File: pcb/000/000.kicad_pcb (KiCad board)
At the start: 4 copper layers, 80 x 71 mm, 155 parts, among them J1 Screw_Terminal_01x10, J2 Screw_Terminal_01x10, Q1 BC846BLT1G, Q10 BC846BLT1G, Q11 BC846BLT1G, Q12 BC846BLT1G, Q13 BC846BLT1G, Q14 BC846BLT1G, Q15 BC846BLT1G, Q16 BC846BLT1G, Q17 BC846BLT1G, Q18 BC846BLT1G, Q19 BC846BLT1G, Q2 BC846BLT1G, Q20 BC846BLT1G, Q21 BC846BLT1G, Q22 BC846BLT1G, Q23 BC846BLT1G, Q24 BC846BLT1G, Q3 BC846BLT1G, Q4 BC846BLT1G, Q5 BC846BLT1G, Q6 BC846BLT1G, Q7 BC846BLT1G, Q8 BC846BLT1G, Q9 BC846BLT1G, SW1 SW_DIP_x08, U1 LM339, U2 LM339, U3 TLP291-4, U4 TLP291-4, U5 RFM-0505S

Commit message: rev 4 commit, works but uses a lot of power. commiting this change before going over to the new design
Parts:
- added J3: Conn_01x03, Connector_PinHeader_2.54mm:PinHeader_1x03_P2.54mm_Vertical, F.Cu at (162.0, 116.8)
- added R69: 10kOhm, Resistor_SMD:R_0603_1608Metric, F.Cu at (168.2, 109.5)
- added R70: 20kOhm, Resistor_SMD:R_0603_1608Metric, F.Cu at (166.8, 109.5)
- moved C3 0.50 mm to (167.8, 104.5)
- moved C4 0.50 mm to (159.5, 103.8)
- moved C5 0.50 mm to (159.5, 112.8)
- moved L1 0.50 mm to (164.2, 103.5)
- moved U5 0.50 mm to (159.5, 108.2)
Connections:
- R59 pad 1: ISO_VCC -> PULLUP
- R60 pad 1: ISO_VCC -> PULLUP
- R61 pad 1: ISO_VCC -> PULLUP
- R62 pad 1: ISO_VCC -> PULLUP
- R63 pad 1: ISO_VCC -> PULLUP
- R64 pad 1: ISO_VCC -> PULLUP
- R65 pad 1: ISO_VCC -> PULLUP
- R66 pad 1: ISO_VCC -> PULLUP
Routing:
- net PULLUP: track 0.00 -> 38.8 mm, vias 0 -> 8
- net ISO_3.3: track 0.00 -> 16.6 mm
- net ISO_GND: track 43.8 -> 46.2 mm
- net GND: track 50.6 -> 51.5 mm
- net ISO_VCC: track 17.1 -> 16.3 mm, vias 9 -> 3

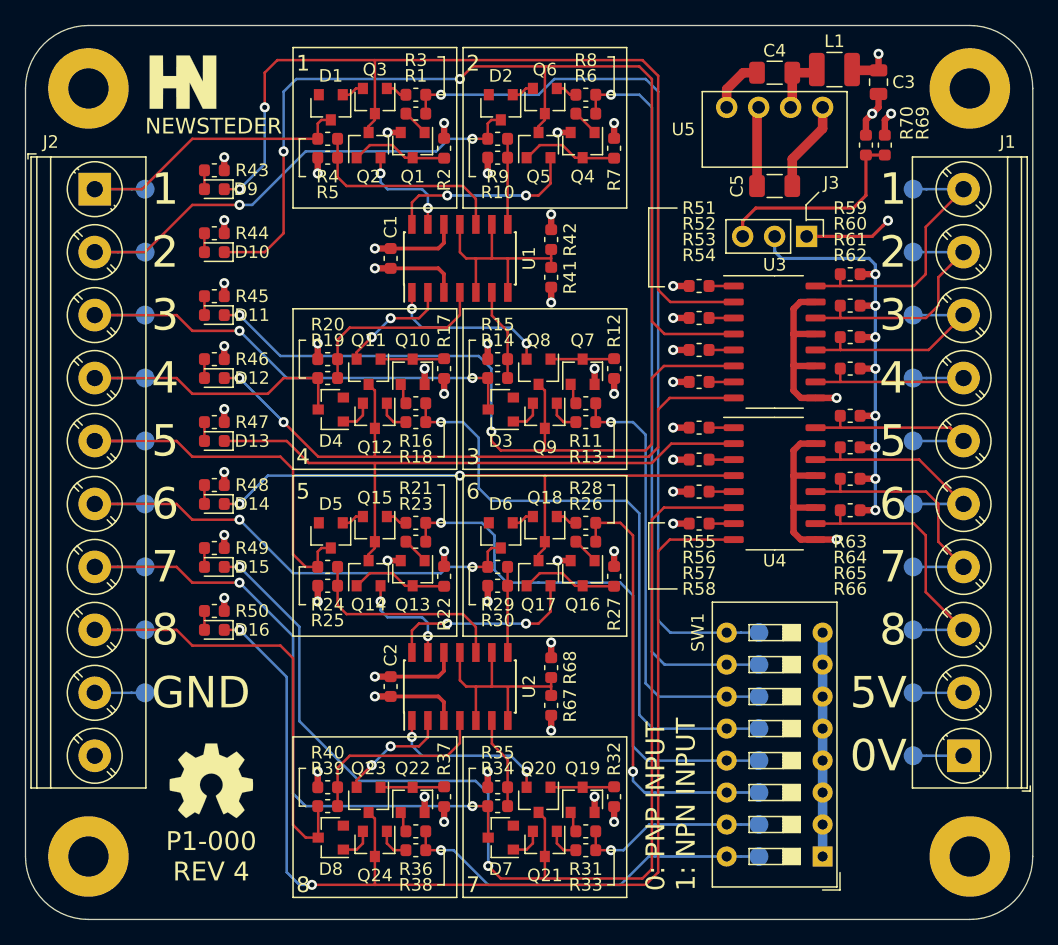
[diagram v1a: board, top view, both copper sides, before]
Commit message: REV 5 of the board, much better power consumption and reponse time but the LDO is no good, only barely works and when you hook up an ammeter it blows the fuck up
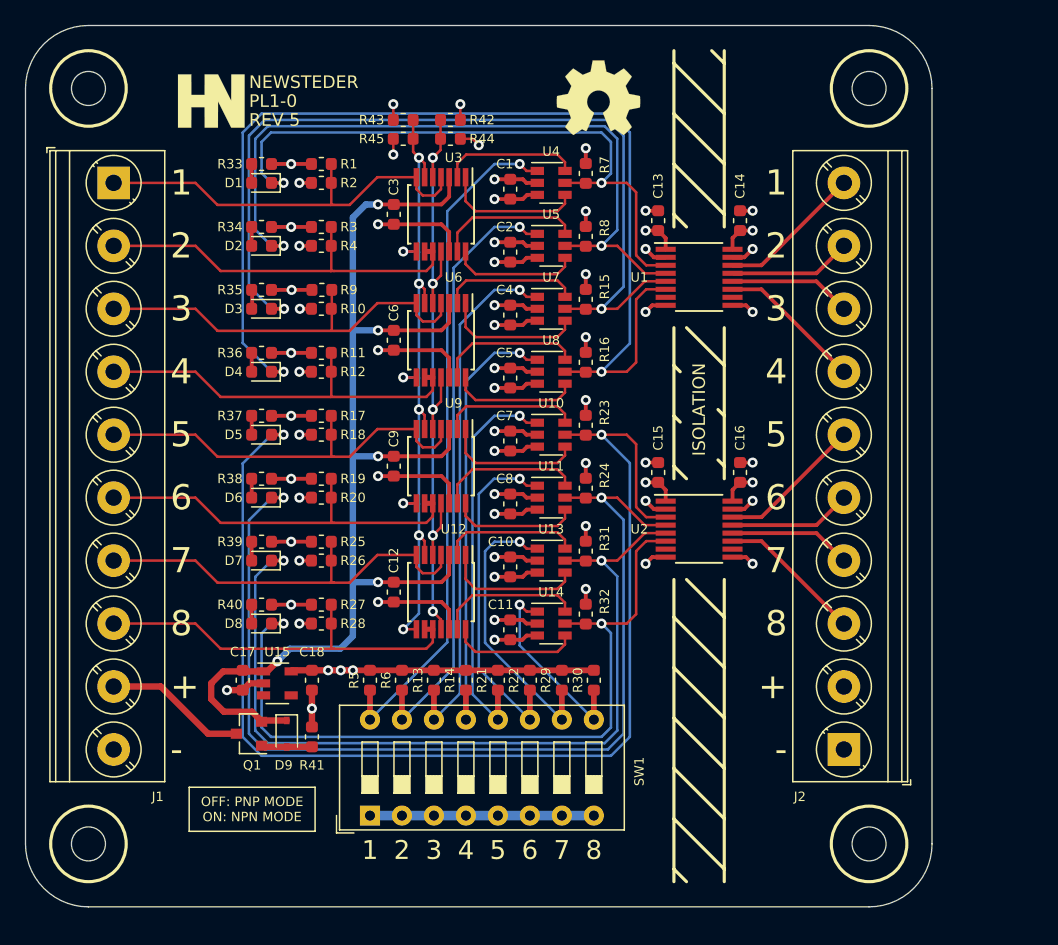
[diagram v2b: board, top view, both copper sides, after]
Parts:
- removed D10, D11, D12, D13, D14, D15, D16: LED, LED_SMD:LED_0603_1608Metric
- removed H1, H2, H3, H4: MountingHole_Pad, MountingHole:MountingHole_3.2mm_M3_Pad
- removed J3: Conn_01x03, Connector_PinHeader_2.54mm:PinHeader_1x03_P2.54mm_Vertical
- removed L1: 22uH, Inductor_SMD:L_1210_3225Metric
- removed Q10, Q11, Q12, Q13, Q14, Q15, Q16, Q17, Q18, Q19, Q2, Q20, Q21, Q22, Q23, Q24, Q3, Q4, Q5, Q6, Q7, Q8, Q9: BC846BLT1G, Package_TO_SOT_SMD:SOT-23
- removed R46, R47, R48, R49, R50, R51, R52, R53, R54, R55, R56, R57, R58: 1kOhm, Resistor_SMD:R_0603_1608Metric
- removed R59, R60, R61, R62, R63, R64, R65, R66, R69: 10kOhm, Resistor_SMD:R_0603_1608Metric
- removed R67: 2k, Resistor_SMD:R_0603_1608Metric
- removed R68: 180, Resistor_SMD:R_0603_1608Metric
- removed R70: 20kOhm, Resistor_SMD:R_0603_1608Metric
- removed TP1, TP10, TP11, TP12, TP13, TP14, TP15, TP16, TP17, TP18, TP19, TP2, TP20, TP21, TP22, TP23, TP24, TP25, TP26, TP27, TP3, TP4, TP5, TP6, TP7, TP8, TP9: TestPoint, TestPoint:TestPoint_Pad_D1.5mm
- added C10: 0.1uF, Capacitor_SMD:C_0603_1608Metric, F.Cu at (138.5, 143.0)
- added C11: 0.1uF, Capacitor_SMD:C_0603_1608Metric, F.Cu at (138.5, 148.0)
- added C12: 0.1uF, Capacitor_SMD:C_0603_1608Metric, F.Cu at (129.2, 145.0)
- added C13: C, Capacitor_SMD:C_0603_1608Metric, F.Cu at (150.2, 115.5)
- added C14: C, Capacitor_SMD:C_0603_1608Metric, F.Cu at (156.8, 115.5)
- added C15: C, Capacitor_SMD:C_0603_1608Metric, F.Cu at (150.2, 135.5)
- added C16: C, Capacitor_SMD:C_0603_1608Metric, F.Cu at (156.8, 135.5)
- added C17: 1.0uF, Capacitor_SMD:C_0603_1608Metric, F.Cu at (117.2, 152.0)
- added C18: 1.5uF, Capacitor_SMD:C_0603_1608Metric, F.Cu at (122.8, 152.0)
- added C6: 0.1uF, Capacitor_SMD:C_0603_1608Metric, F.Cu at (129.2, 125.0)
- added C7: 0.1uF, Capacitor_SMD:C_0603_1608Metric, F.Cu at (138.5, 133.0)
- added C8: 0.1uF, Capacitor_SMD:C_0603_1608Metric, F.Cu at (138.5, 138.0)
- added C9: 0.1uF, Capacitor_SMD:C_0603_1608Metric, F.Cu at (129.2, 135.0)
- added G***: LOGO, newsteder:PL1-0, B.Cu at (136.0, 135.0)
- added REF**: MountingHole_2.7mm_M2.5, MountingHole:MountingHole_2.7mm_M2.5, F.Cu at (167.0, 165.0)
- added REF**: MountingHole_2.7mm_M2.5, MountingHole:MountingHole_2.7mm_M2.5, F.Cu at (167.0, 105.0)
- added REF**: MountingHole_2.7mm_M2.5, MountingHole:MountingHole_2.7mm_M2.5, F.Cu at (105.0, 105.0)
- added REF**: MountingHole_2.7mm_M2.5, MountingHole:MountingHole_2.7mm_M2.5, F.Cu at (105.0, 165.0)
- added U10: STG719STR, Package_TO_SOT_SMD:SOT-23-6, F.Cu at (141.8, 132.5)
- added U11: STG719STR, Package_TO_SOT_SMD:SOT-23-6, F.Cu at (141.8, 137.5)
- added U12: LM339, Package_SO:TSSOP-14_4.4x5mm_P0.65mm, F.Cu at (133.0, 145.0)
- added U13: STG719STR, Package_TO_SOT_SMD:SOT-23-6, F.Cu at (141.8, 142.5)
- added U14: STG719STR, Package_TO_SOT_SMD:SOT-23-6, F.Cu at (141.8, 147.5)
- added U15: TPS70950DBVR, Package_TO_SOT_SMD:SOT-23-5, F.Cu at (120.0, 152.2)
- added U6: LM339, Package_SO:TSSOP-14_4.4x5mm_P0.65mm, F.Cu at (133.0, 125.0)
- added U7: STG719STR, Package_TO_SOT_SMD:SOT-23-6, F.Cu at (141.8, 122.5)
- added U8: STG719STR, Package_TO_SOT_SMD:SOT-23-6, F.Cu at (141.8, 127.5)
- added U9: LM339, Package_SO:TSSOP-14_4.4x5mm_P0.65mm, F.Cu at (133.0, 135.0)
- C3: value 6.8 uF -> 0.1uF; footprint Capacitor_SMD:C_0805_2012Metric -> Capacitor_SMD:C_0603_1608Metric
- C4, C5: value 330pF 1kVDC -> 0.1uF; footprint Capacitor_SMD:C_1206_3216Metric -> Capacitor_SMD:C_0603_1608Metric
- D1, D2, D3, D4, D5, D6, D7, D8: value BAS16LT1G -> LED; footprint Package_TO_SOT_SMD:SOT-23 -> LED_SMD:LED_0603_1608Metric
- D9: value LED -> MM3Z10VT1G; footprint LED_SMD:LED_0603_1608Metric -> Diode_SMD:D_SOD-323
- J1: value Screw_Terminal_01x10 -> INPUT TERMINAL
- J2: value Screw_Terminal_01x10 -> OUTPUT TERMINAL
- Q1: value BC846BLT1G -> ZXMP10A13FTA
- R1, R11, R12, R13, R16, R17, R18, R2, R21, R22, R23, R26, R27, R28, R3, R31, R32, R6, R7, R8: value 1k -> 10kOhm
- R10, R15, R20, R25, R30, R5: value 4.99k -> 10kOhm
- R14, R19, R24, R29, R4, R9: value 45.3k -> 10kOhm
- R33, R36, R37, R38: value 1k -> 1kOhm
- R34, R39: value 45.3k -> 1kOhm
- R35, R40: value 4.99k -> 1kOhm
- R41: value 2k -> 100kOhm
- R42: value 180 -> 6.65kOhm
- R43, R44: value 1kOhm -> 10kOhm
- R45: value 1kOhm -> 6.65kOhm
- SW1: value SW_DIP_x08 -> MODE SELECT SWITCH
- U1, U2: value LM339 -> Si8645BA-B-IU; footprint Package_SO:SOIC-14_3.9x8.7mm_P1.27mm -> Package_SO:QSOP-16_3.9x4.9mm_P0.635mm
- U3: value TLP291-4 -> LM339; footprint Package_SO:SOIC-16_4.55x10.3mm_P1.27mm -> Package_SO:TSSOP-14_4.4x5mm_P0.65mm
- U4: value TLP291-4 -> STG719STR; footprint Package_SO:SOIC-16_4.55x10.3mm_P1.27mm -> Package_TO_SOT_SMD:SOT-23-6
- U5: value RFM-0505S -> STG719STR; footprint newsteder:RFM-0505S -> Package_TO_SOT_SMD:SOT-23-6
- moved J1 81.4 mm to (107.0, 112.5), turned to 270 degrees
- moved J2 74.3 mm to (165.0, 157.5), turned to 90 degrees
- moved REF** 62.4 mm to (145.5, 105.8)
- moved R33 60.3 mm to (118.8, 111.0), turned to 180 degrees
- moved R34 49.7 mm to (118.8, 116.0)
- moved Q1 48.5 mm to (117.8, 156.2), turned to 180 degrees
- moved R6 47.3 mm to (129.9, 152.0), turned to 270 degrees
- moved R35 43.7 mm to (118.8, 121.0)
- moved D9 43.6 mm to (120.8, 156.2), turned to 270 degrees
- moved R5 41.6 mm to (127.4, 152.0), turned to 270 degrees
- moved R41 41.1 mm to (122.8, 156.5)
- moved R36 39.9 mm to (118.8, 126.0), turned to 180 degrees
- moved C3 39.9 mm to (129.2, 115.0)
- moved SW1 36.1 mm to (127.4, 162.8), turned to 90 degrees
- moved C2 35.8 mm to (138.5, 118.0), turned to 270 degrees
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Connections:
- C3 pad 1: ISO_VCC -> +VDC
- C3 pad 2: ISO_GND -> GND
- C4 pad 1: Net-(C4-Pad1) -> +5V
- C4 pad 2: +5V -> GND
- C5 pad 1: ISO_GND -> +5V
- D1 pad 1: Net-(D1-Pad1) -> /UOUT_0
- D1 pad 2: (no net) -> Net-(D1-Pad2)
- D2 pad 1: Net-(D2-Pad1) -> /UOUT_1
- D2 pad 2: (no net) -> Net-(D2-Pad2)
- D3 pad 1: Net-(D3-Pad1) -> /UOUT_2
- D3 pad 2: (no net) -> Net-(D3-Pad2)
- D4 pad 1: Net-(D4-Pad1) -> /UOUT_3
- D4 pad 2: (no net) -> Net-(D4-Pad2)
- D5 pad 1: Net-(D5-Pad1) -> /UOUT_5
- D5 pad 2: (no net) -> Net-(D5-Pad2)
- D6 pad 1: Net-(D6-Pad1) -> /UOUT_6
- D6 pad 2: (no net) -> Net-(D6-Pad2)
- D7 pad 1: Net-(D7-Pad1) -> /UOUT_7
- D7 pad 2: (no net) -> Net-(D7-Pad2)
- D8 pad 1: Net-(D8-Pad1) -> /UOUT_8
- D8 pad 2: (no net) -> Net-(D8-Pad2)
- D9 pad 1: OUTPUT_0 -> +VDC
- J1 pad 1: ISO_GND -> /SIG_0
- J1 pad 10: SIGNAL_0 -> GND
- J1 pad 2: ISO_VCC -> /SIG_1
- J1 pad 3: SIGNAL_7 -> /SIG_2
- J1 pad 4: SIGNAL_6 -> /SIG_3
- J1 pad 5: SIGNAL_5 -> /SIG_4
- J1 pad 6: SIGNAL_4 -> /SIG_5
- J1 pad 7: SIGNAL_3 -> /SIG_6
- J1 pad 8: SIGNAL_2 -> /SIG_7
- J1 pad 9: SIGNAL_1 -> VIN
- J2 pad 1: SENSOR_0 -> LV-
- J2 pad 10: GND -> /OUT_0
- J2 pad 2: SENSOR_1 -> LV+
- J2 pad 3: SENSOR_2 -> /OUT_7
- J2 pad 4: SENSOR_3 -> /OUT_6
- J2 pad 5: SENSOR_4 -> /OUT_5
- J2 pad 6: SENSOR_5 -> /OUT_4
- J2 pad 7: SENSOR_6 -> /OUT_3
- J2 pad 8: SENSOR_7 -> /OUT_2
- J2 pad 9: GND -> /OUT_1
- Q1 pad 1: Net-(Q1-Pad1) -> Net-(D9-Pad2)
- Q1 pad 2: GND -> +VDC
- Q1 pad 3: Net-(Q1-Pad3) -> VIN
- R1 pad 1: Net-(Q1-Pad1) -> +5V
- R1 pad 2: MODE_0 -> /SIG_0
- R10 pad 1: Net-(R10-Pad1) -> /SIG_2
- R11 pad 1: Net-(Q7-Pad1) -> +5V
- R11 pad 2: MODE_2 -> /SIG_3
- R12 pad 1: Net-(Q7-Pad3) -> /SIG_3
- R12 pad 2: +5V -> GND
- R13 pad 1: Net-(Q9-Pad1) -> +5V
- R14 pad 1: Net-(R14-Pad1) -> +5V
- R14 pad 2: SENSOR_2 -> MODE_3
- R15 pad 1: Net-(R14-Pad1) -> +5V
- R15 pad 2: GND -> /UOUT_2
- R16 pad 1: Net-(Q10-Pad1) -> +5V
- R16 pad 2: MODE_3 -> /UOUT_3
- R17 pad 1: Net-(Q10-Pad3) -> +5V
- R17 pad 2: +5V -> /SIG_4
- R18 pad 1: Net-(Q12-Pad1) -> /SIG_4
- R18 pad 2: MODE_3 -> GND
- R19 pad 1: Net-(R19-Pad1) -> +5V
- R19 pad 2: SENSOR_3 -> /SIG_5
- R2 pad 1: Net-(Q1-Pad3) -> /SIG_0
- R2 pad 2: +5V -> GND
- R20 pad 1: Net-(R19-Pad1) -> /SIG_5
- R21 pad 1: Net-(Q13-Pad1) -> +5V
- R22 pad 1: Net-(Q13-Pad3) -> +5V
- R22 pad 2: +5V -> MODE_5
- R23 pad 1: Net-(Q15-Pad1) -> +5V
- R23 pad 2: MODE_4 -> /UOUT_5
- R24 pad 1: Net-(R24-Pad1) -> +5V
- R24 pad 2: SENSOR_4 -> /UOUT_6
- R25 pad 1: Net-(R24-Pad1) -> +5V
- R25 pad 2: GND -> /SIG_6
- R26 pad 1: Net-(Q16-Pad1) -> /SIG_6
- R26 pad 2: MODE_5 -> GND
- R27 pad 1: Net-(Q16-Pad3) -> +5V
- R27 pad 2: +5V -> /SIG_7
- R28 pad 1: Net-(Q18-Pad1) -> /SIG_7
- R28 pad 2: MODE_5 -> GND
- R29 pad 1: Net-(R29-Pad1) -> +5V
- R29 pad 2: SENSOR_5 -> MODE_6
- R3 pad 1: Net-(Q3-Pad1) -> +5V
- R3 pad 2: MODE_0 -> /SIG_1
- R30 pad 1: Net-(R29-Pad1) -> +5V
- R30 pad 2: GND -> MODE_7
- R31 pad 1: Net-(Q19-Pad1) -> +5V
- R31 pad 2: MODE_6 -> /UOUT_7
- R32 pad 1: Net-(Q19-Pad3) -> +5V
- R32 pad 2: +5V -> /UOUT_8
- R33 pad 1: Net-(Q21-Pad1) -> +5V
- R33 pad 2: MODE_6 -> Net-(D1-Pad2)
- R34 pad 1: Net-(R34-Pad1) -> +5V
- R34 pad 2: SENSOR_6 -> Net-(D2-Pad2)
- R35 pad 1: Net-(R34-Pad1) -> +5V
- R35 pad 2: GND -> Net-(D3-Pad2)
- R36 pad 1: Net-(Q22-Pad1) -> +5V
- R36 pad 2: MODE_7 -> Net-(D4-Pad2)
- R37 pad 1: Net-(Q22-Pad3) -> +5V
- R37 pad 2: +5V -> Net-(D5-Pad2)
- R38 pad 1: Net-(Q24-Pad1) -> +5V
- R38 pad 2: MODE_7 -> Net-(D6-Pad2)
- R39 pad 1: Net-(R39-Pad1) -> +5V
- R39 pad 2: SENSOR_7 -> Net-(D7-Pad2)
- R4 pad 1: Net-(R4-Pad1) -> /SIG_1
- R4 pad 2: SENSOR_0 -> GND
- R40 pad 1: Net-(R39-Pad1) -> +5V
- R40 pad 2: GND -> Net-(D8-Pad2)
- R41 pad 1: +5V -> Net-(D9-Pad2)
- R41 pad 2: 0.413V_A -> GND
- R42 pad 1: 0.413V_A -> +5V
- R42 pad 2: GND -> 3.0V
- R43 pad 1: Net-(D9-Pad2) -> +5V
- R43 pad 2: +5V -> 2.0V
- R44 pad 1: Net-(D10-Pad2) -> 3.0V
- R44 pad 2: +5V -> GND
- R45 pad 1: Net-(D11-Pad2) -> 2.0V
- R45 pad 2: +5V -> GND
- R5 pad 1: Net-(R4-Pad1) -> +5V
- R5 pad 2: GND -> MODE_0
- R6 pad 1: Net-(Q4-Pad1) -> +5V
- R7 pad 1: Net-(Q4-Pad3) -> +5V
- R7 pad 2: +5V -> /UOUT_0
- R8 pad 1: Net-(Q6-Pad1) -> +5V
- R8 pad 2: MODE_1 -> /UOUT_1
- R9 pad 1: Net-(R10-Pad1) -> +5V
- R9 pad 2: SENSOR_1 -> /SIG_2
- SW1 pad 1: +5V -> GND
- SW1 pad 10: MODE_1 -> MODE_6
- SW1 pad 11: MODE_2 -> MODE_5
- SW1 pad 12: MODE_3 -> MODE_4
- SW1 pad 13: MODE_4 -> MODE_3
- SW1 pad 14: MODE_5 -> MODE_2
- SW1 pad 15: MODE_6 -> MODE_1
- SW1 pad 16: MODE_7 -> MODE_0
- SW1 pad 2: +5V -> GND
- SW1 pad 3: +5V -> GND
- SW1 pad 4: +5V -> GND
- SW1 pad 5: +5V -> GND
- SW1 pad 6: +5V -> GND
- SW1 pad 7: +5V -> GND
- SW1 pad 8: +5V -> GND
- SW1 pad 9: MODE_0 -> MODE_7
- U1 pad 1: Net-(Q8-Pad2) -> +5V
- U1 pad 10: Net-(R4-Pad1) -> Net-(U1-Pad10)
- U1 pad 11: 0.413V_A -> /OUT_3
- U1 pad 12: GND -> /OUT_2
- U1 pad 13: Net-(Q2-Pad2) -> /OUT_1
- U1 pad 14: Net-(Q5-Pad2) -> /OUT_0
- U1 pad 2: Net-(Q11-Pad2) -> GND
- U1 pad 3: +5V -> /UOUT_0
- U1 pad 4: Net-(R19-Pad1) -> /UOUT_1
- U1 pad 5: 0.413V_A -> /UOUT_2
- U1 pad 6: Net-(R14-Pad1) -> /UOUT_3
- U1 pad 7: 0.413V_A -> Net-(U1-Pad7)
- U1 pad 8: Net-(R10-Pad1) -> GND
- U1 pad 9: 0.413V_A -> LV-
- U2 pad 1: Net-(Q20-Pad2) -> +5V
- U2 pad 10: Net-(R24-Pad1) -> Net-(U2-Pad10)
- U2 pad 11: 0.413V_B -> /OUT_7
- U2 pad 12: GND -> /OUT_6
- U2 pad 13: Net-(Q14-Pad2) -> /OUT_5
- U2 pad 14: Net-(Q17-Pad2) -> /OUT_4
- U2 pad 2: Net-(Q23-Pad2) -> GND
- U2 pad 3: +5V -> /UOUT_5
- U2 pad 4: Net-(R39-Pad1) -> /UOUT_6
- U2 pad 5: 0.413V_B -> /UOUT_7
- U2 pad 6: Net-(R34-Pad1) -> /UOUT_8
- U2 pad 7: 0.413V_B -> Net-(U2-Pad7)
- U2 pad 8: Net-(R29-Pad1) -> GND
- U2 pad 9: 0.413V_B -> LV-
- U3 pad 1: Net-(R51-Pad1) -> Net-(U3-Pad1)
- U3 pad 10: SIGNAL_3 -> /SIG_1
- U3 pad 11: ISO_GND -> 3.0V
- U3 pad 12: SIGNAL_2 -> GND
- U3 pad 13: ISO_GND -> Net-(U3-Pad13)
- U3 pad 14: SIGNAL_1 -> Net-(U3-Pad14)
- U3 pad 2: OUTPUT_0 -> Net-(U3-Pad2)
- U3 pad 3: Net-(R52-Pad1) -> +VDC
- U3 pad 4: OUTPUT_1 -> /SIG_0
- U3 pad 5: Net-(R53-Pad1) -> 3.0V
- U3 pad 6: OUTPUT_2 -> 2.0V
- U3 pad 7: Net-(R54-Pad1) -> /SIG_0
- U3 pad 8: OUTPUT_3 -> 2.0V
- U3 pad 9: ISO_GND -> /SIG_1
- U4 pad 1: Net-(R55-Pad1) -> MODE_0
- U4 pad 2: OUTPUT_4 -> +5V
- U4 pad 3: Net-(R56-Pad1) -> GND
- U4 pad 4: OUTPUT_5 -> Net-(U3-Pad1)
- U4 pad 5: Net-(R57-Pad1) -> /UOUT_0
- U4 pad 6: OUTPUT_6 -> Net-(U3-Pad2)
- U5 pad 1: ISO_GND -> MODE_1
- U5 pad 2: Net-(C4-Pad1) -> +5V
- U5 pad 4: +5V -> Net-(U3-Pad14)
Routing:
- net /UOUT_5: track 0.00 -> 97.4 mm, vias 0 -> 2
- net +VDC: track 0.00 -> 92.4 mm, vias 0 -> 5
- net OUTPUT_6: track 92.4 -> 0.00 mm, vias 2 -> 0
- net OUTPUT_7: track 90.2 -> 0.00 mm, vias 2 -> 0
- net /UOUT_3: track 0.00 -> 87.4 mm, vias 0 -> 2
- net /UOUT_6: track 0.00 -> 80.6 mm, vias 0 -> 2
- net OUTPUT_1: track 78.7 -> 0.00 mm, vias 2 -> 0
- net OUTPUT_0: track 72.8 -> 0.00 mm, vias 2 -> 0
- net /UOUT_2: track 0.00 -> 70.6 mm, vias 0 -> 2
- net /UOUT_7: track 0.00 -> 68.5 mm, vias 0 -> 2
- net /UOUT_8: track 0.00 -> 61.1 mm, vias 0 -> 2
- net OUTPUT_2: track 59.6 -> 0.00 mm, vias 2 -> 0
- net /UOUT_1: track 0.00 -> 58.5 mm, vias 0 -> 2
- net 2.0V: track 0.00 -> 56.1 mm, vias 0 -> 8
- net 3.0V: track 0.00 -> 55.6 mm, vias 0 -> 5
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- added copper zone on In2.Cu, net LV+
- added copper zone on In1.Cu, net LV-
- removed copper zone on In1.Cu, net ISO_GND
- removed copper zone on In2.Cu, net ISO_VCC
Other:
- board size 80 x 71 mm -> 72 x 70 mm
- board text added: "+"
- board text added: "-"
- board text added: "ISOLATION"
- board text added: "OFF: PNP MODE ON: NPN MODE"
- board text added: "PL1-0"
- board text added: "REV 5"
- board text removed: "0: PNP INPUT 1: NPN INPUT"
- board text removed: "0V"
- board text removed: "5V"
- board text removed: "GND"
- board text removed: "P1-000 REV 4"
